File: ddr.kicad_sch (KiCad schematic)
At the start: 69 parts, among them U801 MT41K256M16TW

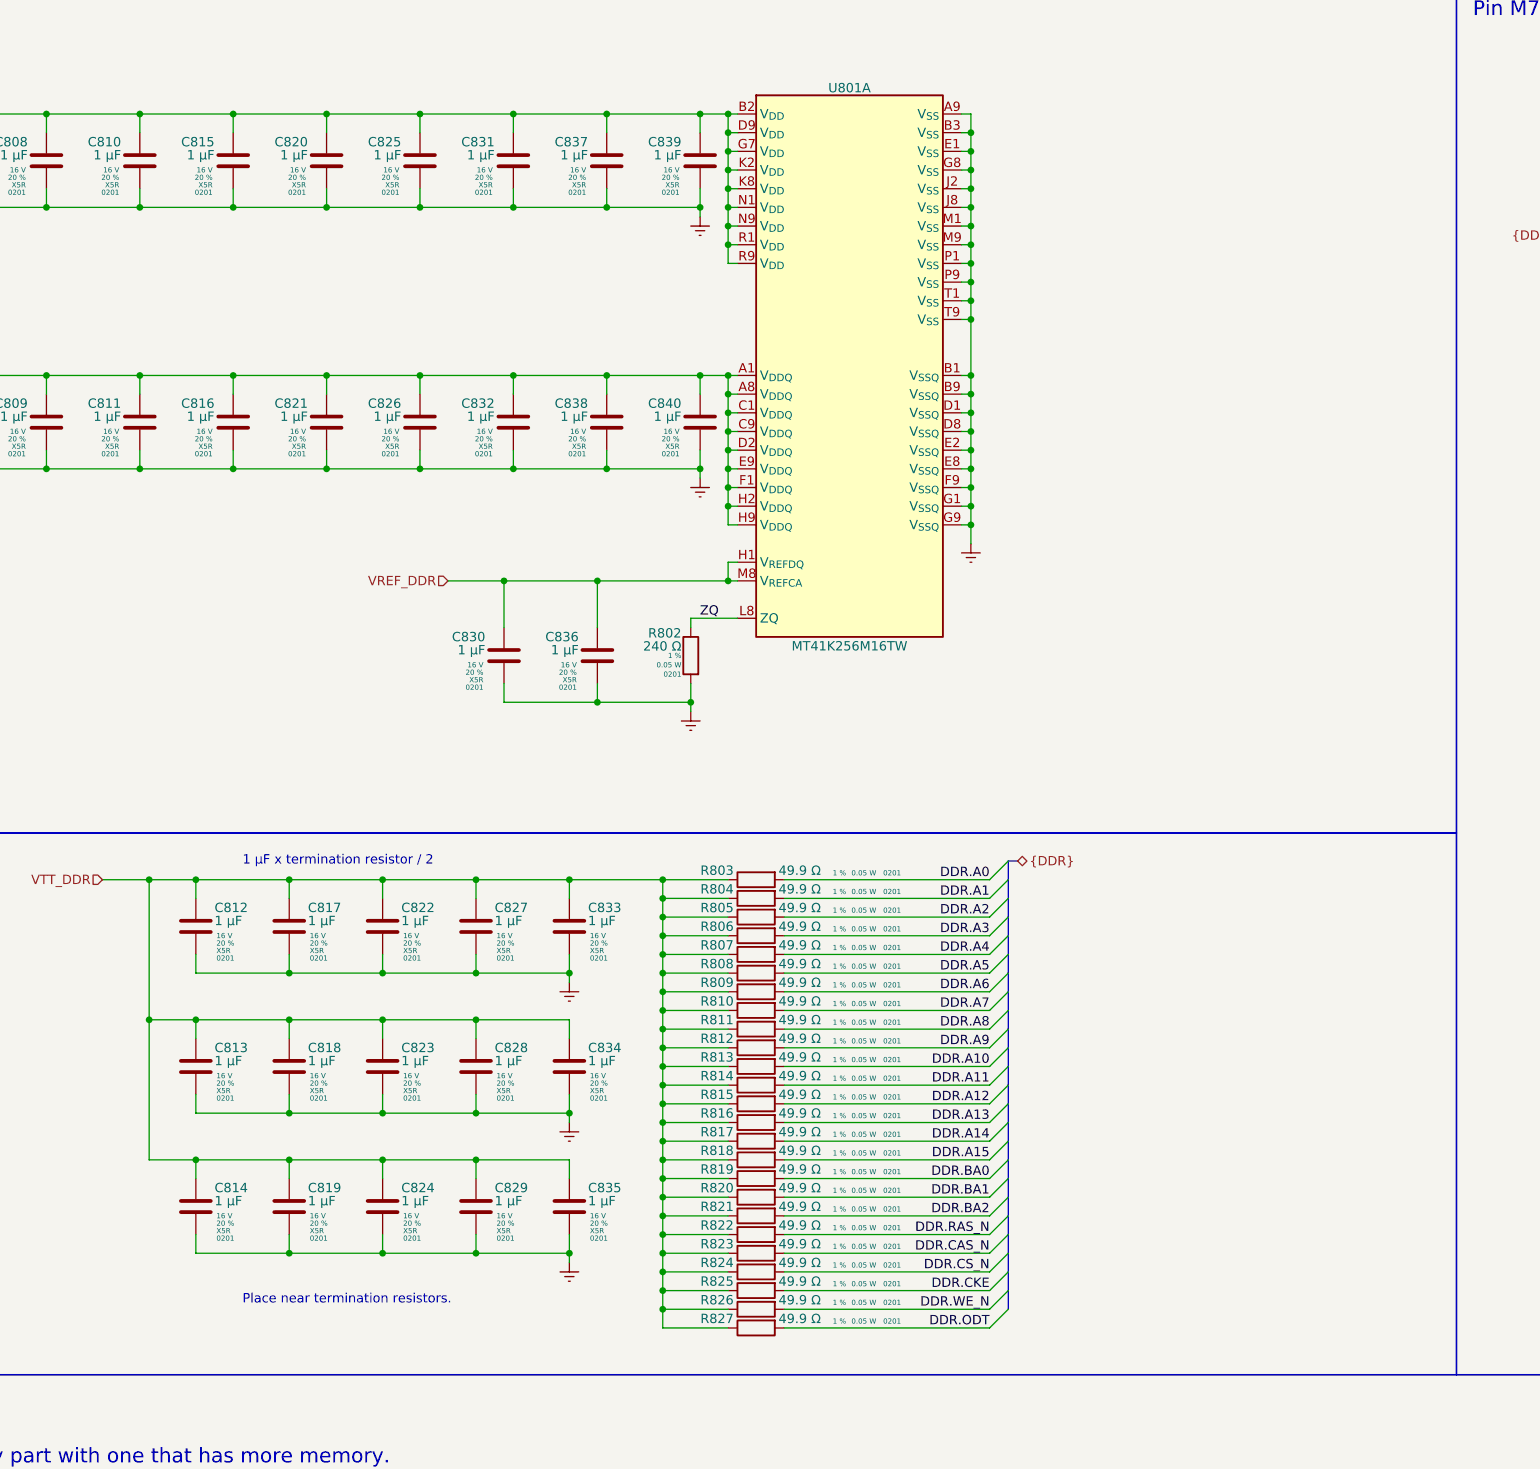
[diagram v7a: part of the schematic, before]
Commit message: Initial VTT termination layout
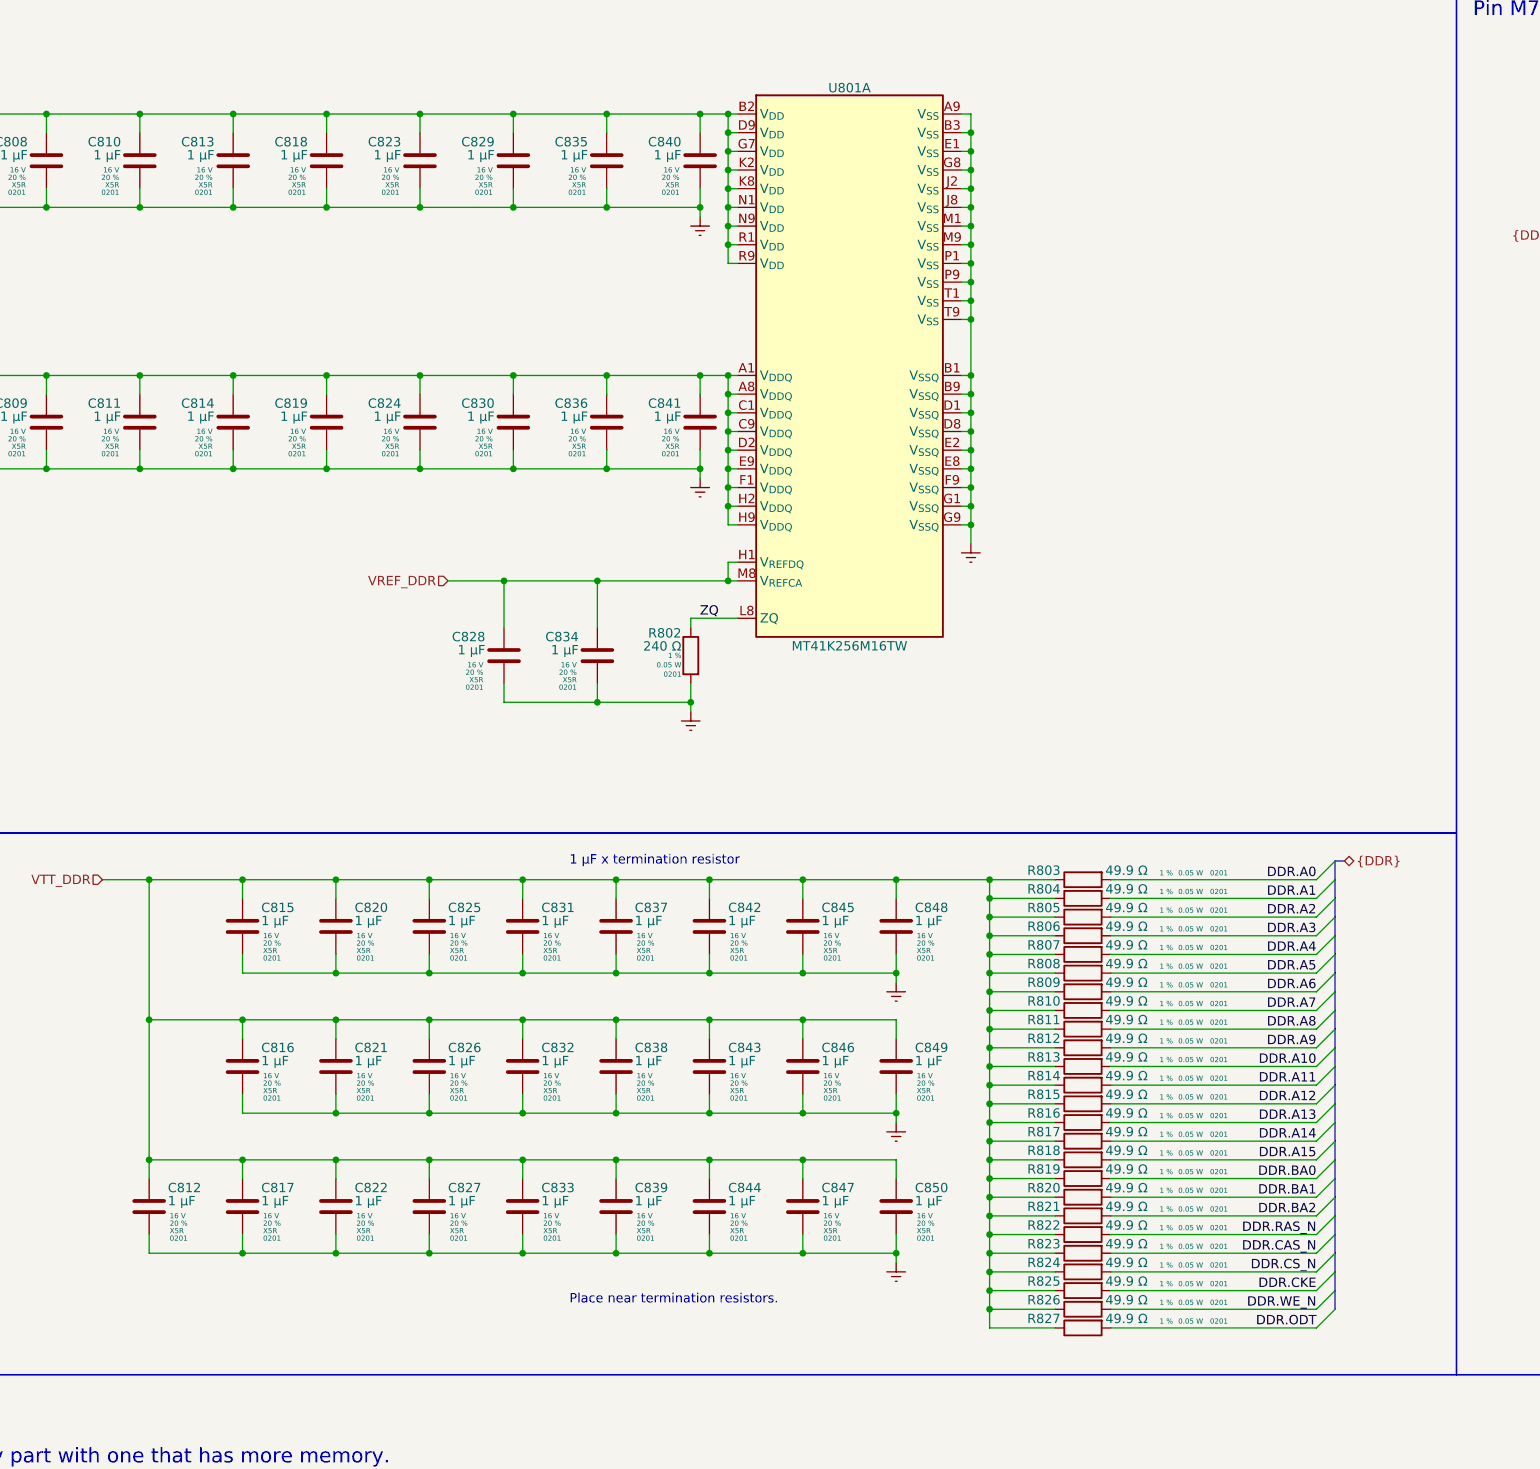
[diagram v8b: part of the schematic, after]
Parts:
- added C812, C815, C816, C817, C820, C821, C822, C825, C826, C827: 1 µF, perfect_footprints:C_0201_0603Metric, symbol Device:C
- renumbered C815 to C813, C816 to C814, C820 to C818, C821 to C819, C825 to C823, C826 to C824, C830 to C828, C831 to C829, C832 to C830, C812 to C831, C813 to C832, C814 to C833, C836 to C834, C837 to C835, C838 to C836, C817 to C837, C818 to C838, C819 to C839, C839 to C840, C840 to C841, C822 to C842, C823 to C843, C824 to C844, C827 to C845, C828 to C846, C829 to C847, C833 to C848, C834 to C849, C835 to C850
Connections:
- net GND: now also C812.2, C815.2, C816.2, C817.2, C820.2, C821.2, C822.2, C825.2, C826.2, C827.2
- net VTT_DDR: now also C812.1, C815.1, C816.1, C817.1, C820.1, C821.1, C822.1, C825.1, C826.1, C827.1
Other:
- note added: "1 µF x termination resistor"
- note removed: "1 µF x termination resistor / 2"
- moved on the sheet: C831, C832, C833, C837, C838, C839, C842, C843, C844, C845, C846, C847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
